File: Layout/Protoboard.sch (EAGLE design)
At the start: 3 parts

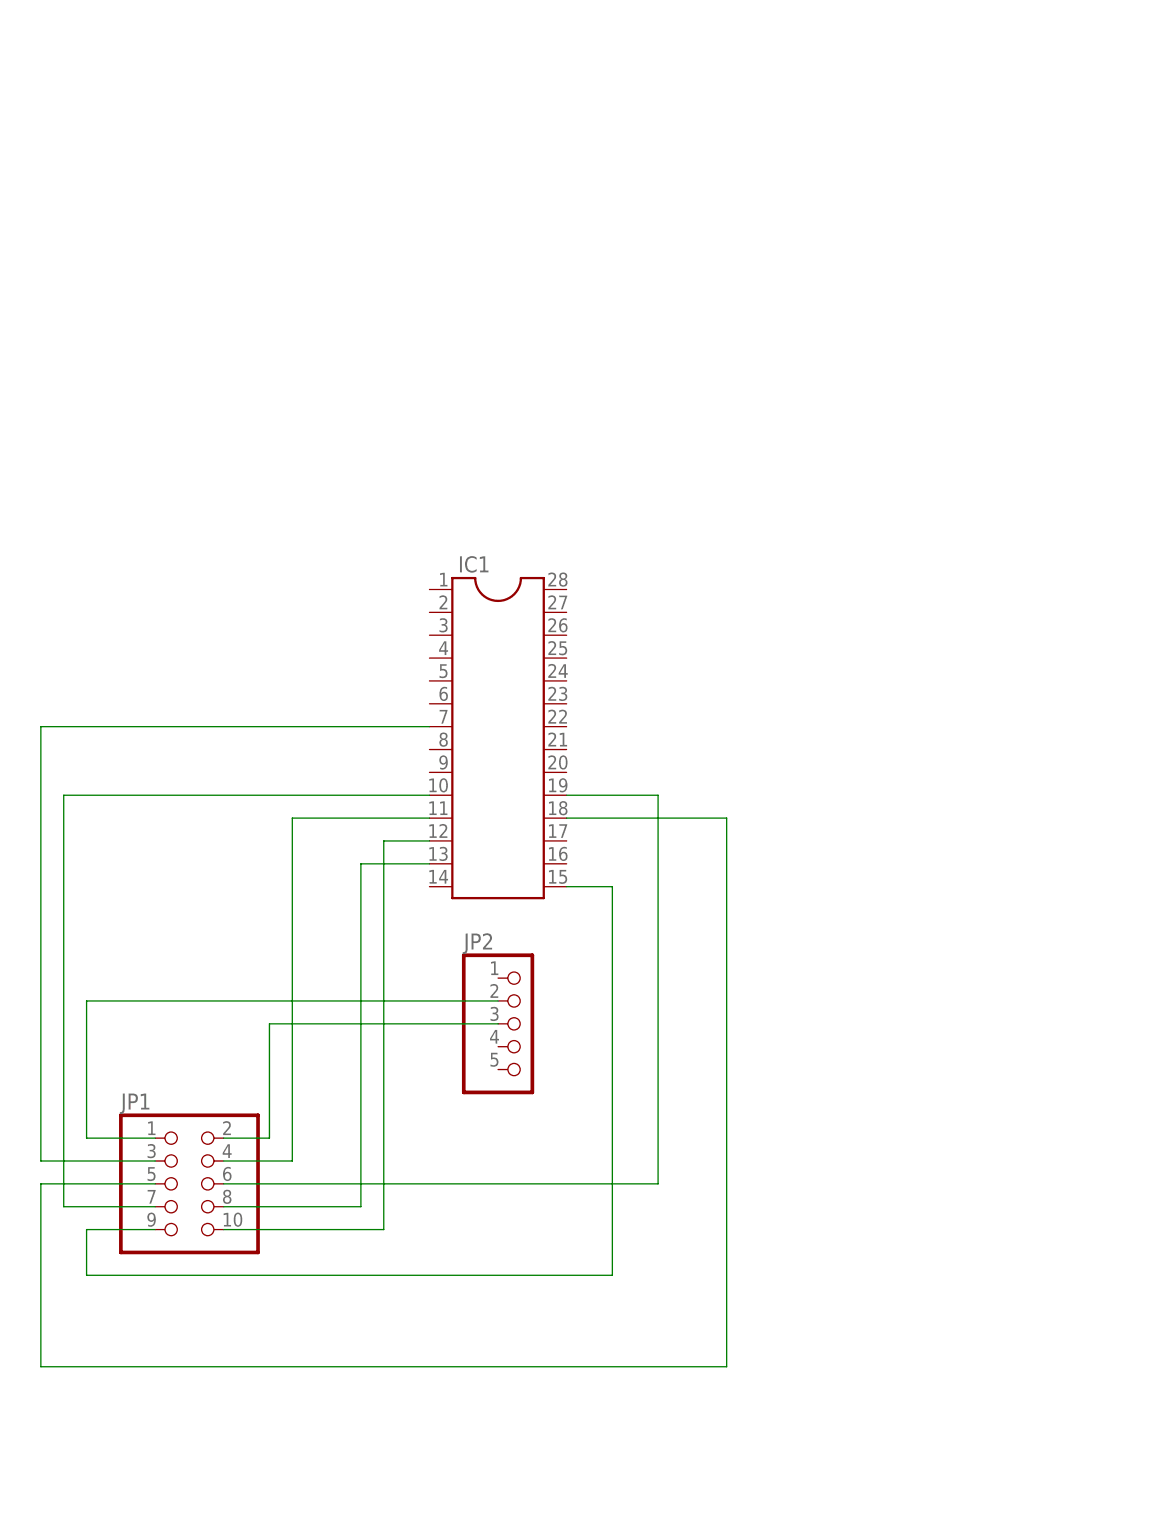
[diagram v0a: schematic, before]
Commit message: add display enable/disable + images
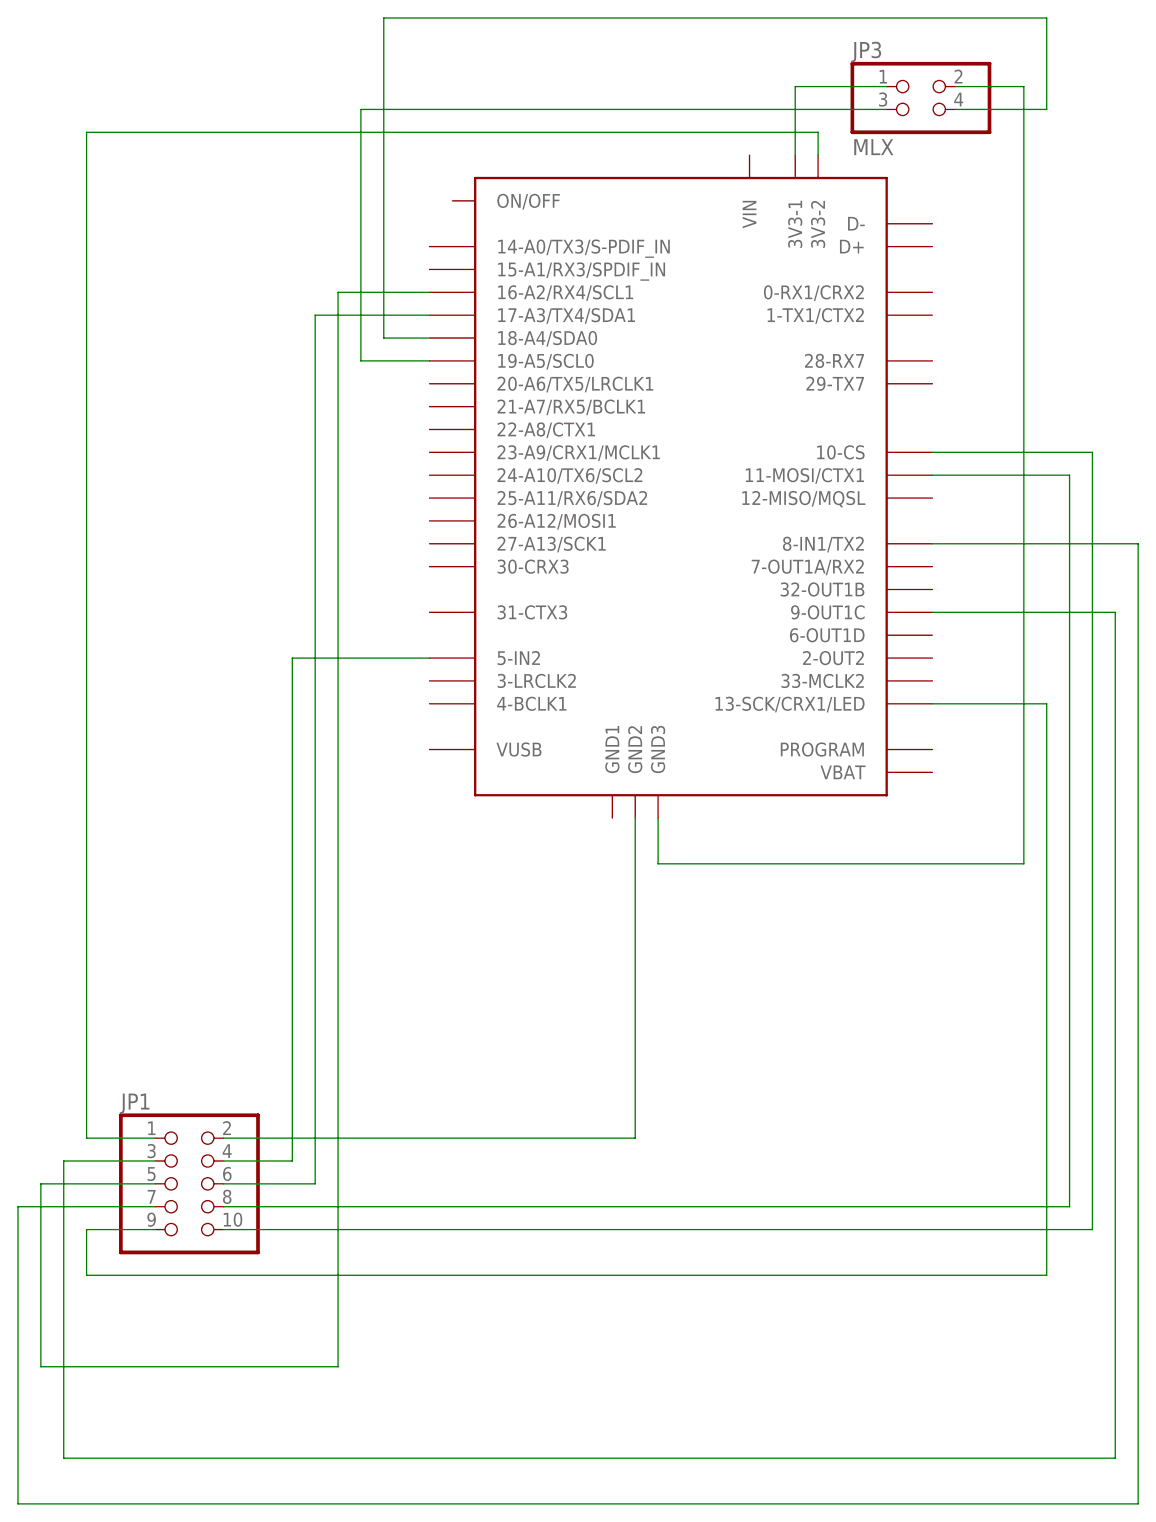
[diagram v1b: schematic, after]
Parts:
- removed IC1: (no value), ic-package:DIL28
- removed JP2: (no value), pinhead:PINHD-1X5
- added JP3: MLX, pinhead:PINHD-2X2
- added U$1: TEENSY40, teensy:TEENSY40
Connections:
- removed net N$9: IC1.7, JP1.3
- new net N$11: JP1.8, U$1.11-MOSI/CTX1
- new net N$12: JP1.10, U$1.10-CS
- new net N$13: JP3.4, U$1.18-A4/SDA0
- new net N$14: JP3.3, U$1.19-A5/SCL0
- new net N$15: JP1.3, U$1.9-OUT1C
- net N$1: now also U$1.GND2; no longer JP2.3
- net N$10: now also U$1.5-IN2; no longer IC1.11
- net N$2: now also U$1.3V3-2; no longer JP2.2
- net N$3: now also JP3.1, U$1.3V3-1; no longer IC1.12, JP1.10
- net N$4: now also U$1.13-SCK/CRX1/LED; no longer IC1.15
- net N$5: now also JP3.2, U$1.GND3; no longer IC1.13, JP1.8
- net N$6: now also U$1.8-IN1/TX2; no longer IC1.10
- net N$7: now also U$1.16-A2/RX4/SCL1; no longer IC1.18
- net N$8: now also U$1.17-A3/TX4/SDA1; no longer IC1.19
